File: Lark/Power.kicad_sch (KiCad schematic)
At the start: 0 parts

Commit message: added power section to schematic
It needs revised, due to thermal issue. Specifically in regards to my soft start circuit, the mosfet wont be able to handle the power dissipated during a slow turn on.
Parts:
- added C20, C23, C29: 0.1µF, Murata Electronics:C_0603, symbol Murata Electronics:Capacitor
- added C21: 4.7µF, Murata Electronics:C_0603, symbol Murata Electronics:Capacitor
- added C22: 22µF, Murata Electronics:C_0603, symbol Murata Electronics:Capacitor
- added C24: 6800pF, Murata Electronics:C_0603, symbol Murata Electronics:Capacitor
- added C25: 18pF, Murata Electronics:C_0603, symbol Murata Electronics:Capacitor
- added C26, C27, C28, C32: 22µF, TDK Corporation:C2012X5R1V226M125AC, symbol TDK Corporation:C2012X5R1V226M125AC
- added C30, C31: 10µF, Murata Electronics:C_0603, symbol Murata Electronics:Capacitor
- added D17: SS26FL, onsemi:SS26FL, symbol onsemi:SS26FL
- added D18: LTST-C171GKT, Lite-On Inc:LED_0805, symbol Lite-On Inc:LTST-C171GKT
- added F1: 7A Slow Blow, SCHURTER Inc:3413.0326.22, symbol SCHURTER Inc:3413.0326.22
- added J8: 54-00128, Tensility International Corp:54-00128, symbol Tensility International Corp:54-00128
- added L1: 15µH, TDK Corporation:CLF5030NIT-150M-D, symbol TDK Corporation:CLF5030NIT-150M-D
- added L2: 4.7µH, TDK Corporation:CLF7045NIT-4R7N-D, symbol TDK Corporation:CLF7045NIT-4R7N-D
- added Q1: SISS65DN-T1-GE3, Vishay Siliconix:SISS65DN-T1-GE3, symbol Vishay Siliconix:SISS65DN-T1-GE3
- added Q2: MMBT2222A-7-F, Diodes Incorporated:MMBT2222A-7-F, symbol Diodes Incorporated:MMBT2222A-7-F
- added R43, R45: 15kΩ, Stackpole:R_0603, symbol Stackpole:Resistor
- added R44: 51kΩ, Stackpole:R_0603, symbol Stackpole:Resistor
- added R46: 100kΩ, Stackpole:R_0603, symbol Stackpole:Resistor
- added R47: 402kΩ, Stackpole:R_0603, symbol Stackpole:Resistor
- added R48, R53: 10KΩ, Stackpole:R_0603, symbol Stackpole:Resistor
- added R49: 20KΩ, Stackpole:R_0603, symbol Stackpole:Resistor
- added R50: 100KΩ, Stackpole:R_0603, symbol Stackpole:Resistor
- added R51: 1KΩ, Stackpole:R_0603, symbol Stackpole:Resistor
- added R52: 220Ω, Stackpole:R_2512, symbol Stackpole:Resistor
- added TP10, TP11, TP12, TP8, TP9: TestPoint, TestPoint:TestPoint_Pad_D1.0mm, symbol Connector:TestPoint
- added U11: BD9G102G-LBTR, ROHM:BD9G102G-LBTR, symbol ROHM:BD9G102G-LBTR
- added U12: BD9E302EFJ-E2, ROHM:BD9E302EFJ-E2, symbol ROHM:BD9E302EFJ-E2
- added U13: LD39200PU33R, STMicroelectronics:LD39200PU33R, symbol STMicroelectronics:LD39200PU33R
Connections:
- new net: F1.1, J8.1
- new net: C32.2, Q1.4 (G), R48.2, R49.1
- new net: Q2.3 (C), R49.2
- new net: C24.1, R45.1
- new net: C20.2, D17.1 (K), L1.1, U11.6 (LX)
- new net: Q2.1 (B), R51.2
- new net: C20.1, U11.1 (BST)
- new net: D18.1 (K), R53.1
- new net +24V: C28.1, C29.2, D18.2 (A), Q1.5 (D1), Q1.6 (D2), Q1.7 (D3), Q1.8 (D4), R52.1, TP11.1, U12.2 (VIN), U12.3 (EN)
- new net +24VBC: C21.1, C32.1, F1.2, Q1.1 (S1), Q1.2 (S2), Q1.3 (S3), R48.1, TP10.1, U11.4 (EN), U11.5 (VCC)
- new net +3.3V: C31.1, TP8.1, U13.1 (OUT), U13.2 (SENSE)
- new net +3.3VBC: C22.1, L1.2, R44.1, TP12.1
- new net +4V: C25.2, C26.1, C27.1, C30.1, L2.1, R47.1, TP9.1, U13.5 (EN), U13.6 (IN)
- new net BOOT: C23.1, U12.1 (BOOT)
- new net COMP: C24.2, U12.6 (COMP)
- new net Drain: J8.3, R52.2
- new net FB_1: R43.1, R44.2, U11.3 (FB)
- new net FB_2: C25.1, R46.1, R47.2, U12.5 (FB)
- new net GND: C21.2, C22.2, C26.2, C27.2, C28.2, C29.1, C30.2, C31.2, D17.2 (A), J8.2, Q2.2 (E), R43.2, R45.2, R46.2, R50.2, R53.2, U11.2 (GND), U12.4 (AGND), U12.7 (PGND), U12.9 (EP), U13.3 (GND), U13.7 (EP)
- new net PWR_EN: R50.1, R51.1
- new net SW: C23.2, L2.2, U12.8 (SW)
- no-connect marks 0 -> 1
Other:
- note added: "6800µF Bulk Cap Drain Time 5 Sec @ 100mA"
- note added: "ATTiny Boot Controller Supply"
- note added: "Main Buck Regulator"
- note added: "Main Linear Voltage Regulator"
- note added: "Power Entry"
- note added: "Power Test Points"

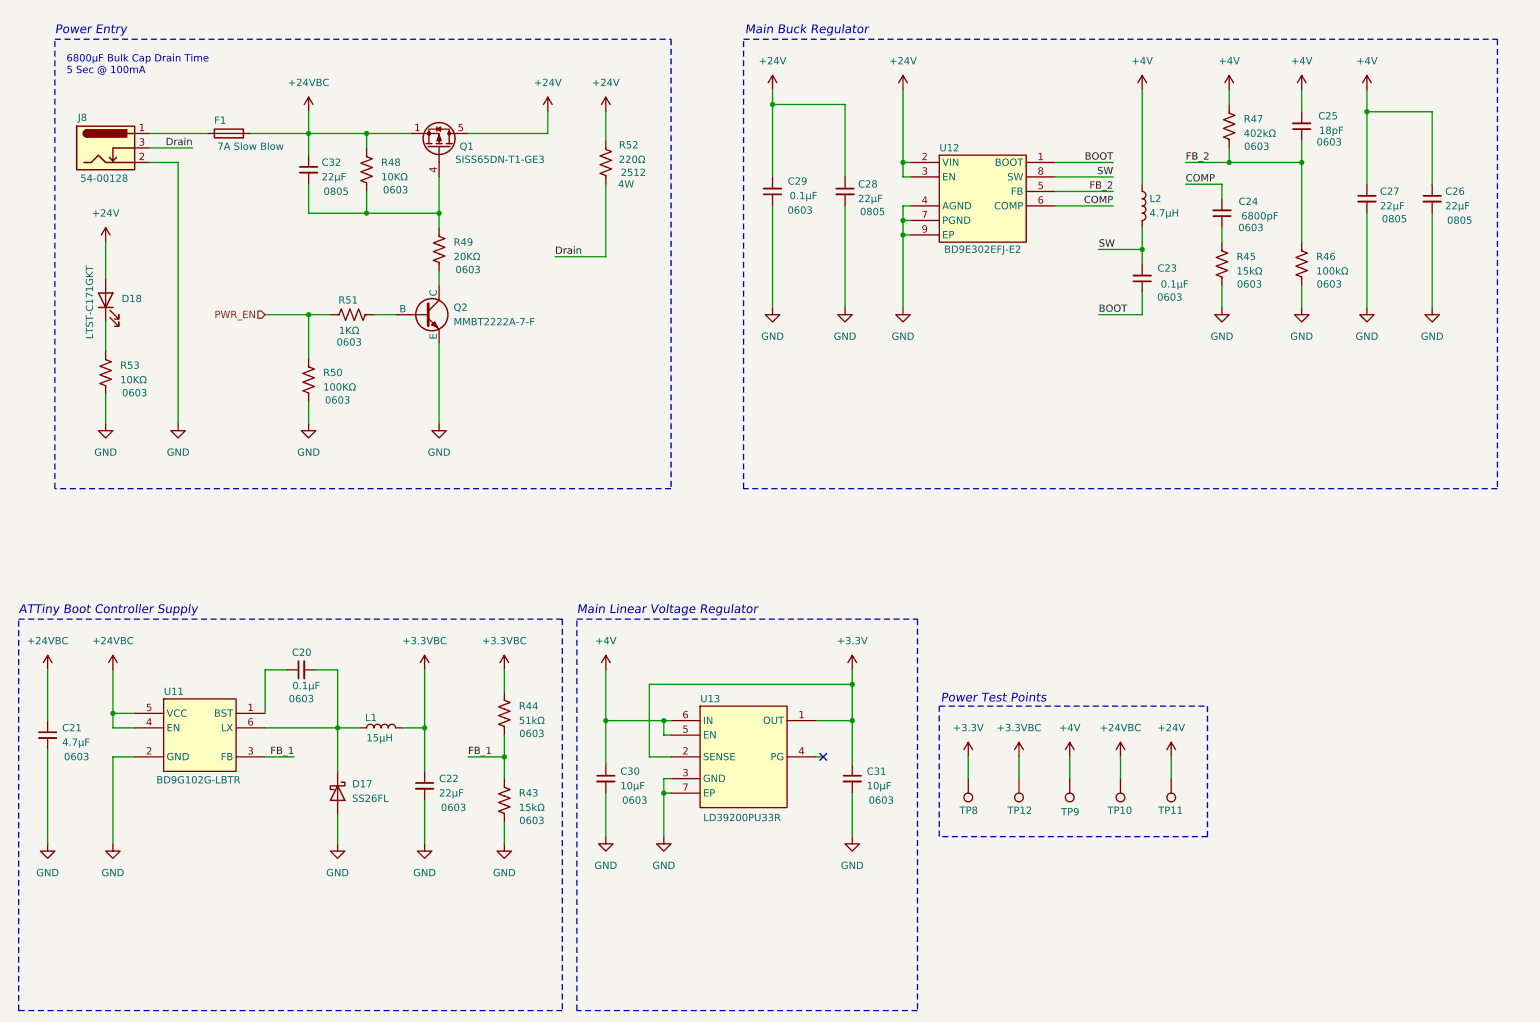
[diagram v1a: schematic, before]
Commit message: update, WIP
- Reannotated schematic.
- Added STM32 device.
- Fixed High-side switch (removed soft-start cap for device safety).
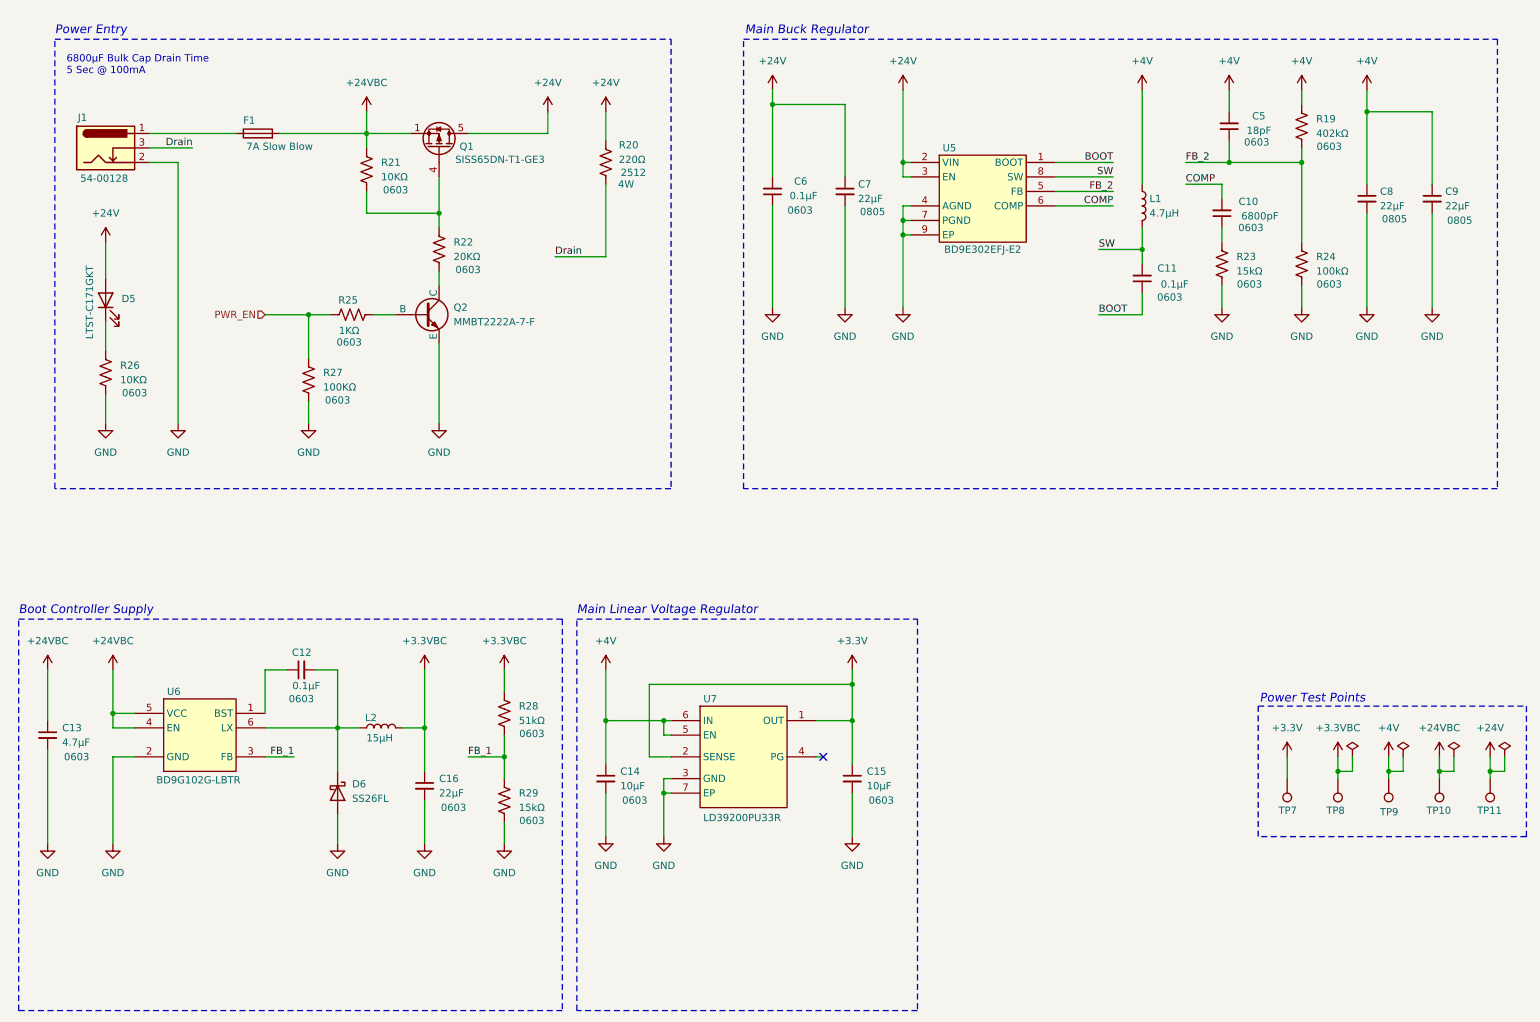
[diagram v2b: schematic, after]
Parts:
- removed C32: 22µF, TDK Corporation:C2012X5R1V226M125AC, symbol TDK Corporation:C2012X5R1V226M125AC
- renumbered C24 to C10, C23 to C11, C20 to C12, C21 to C13, C30 to C14, C31 to C15, C22 to C16, C25 to C5, C29 to C6, C28 to C7, C27 to C8, C26 to C9, D18 to D5, D17 to D6, J8 to J1, L2 to L1, L1 to L2, R47 to R19, R52 to R20, R48 to R21, R49 to R22, R45 to R23, R46 to R24, R51 to R25, R53 to R26, R50 to R27, R44 to R28, R43 to R29, TP8 to TP7, TP12 to TP8, U12 to U5, U11 to U6, U13 to U7
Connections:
- net GND: now also J1.SH1, J1.SH2
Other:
- note added: "Boot Controller Supply"
- note removed: "ATTiny Boot Controller Supply"
- moved on the sheet: C5, F1, R19, TP10, TP11, TP7, TP8, TP9

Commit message: Updated schematic, WIP
- Added NOR flash part.
- Added new CubeMX config file.
- Reannotated the schematic.
- Made some more connections to the MCU.
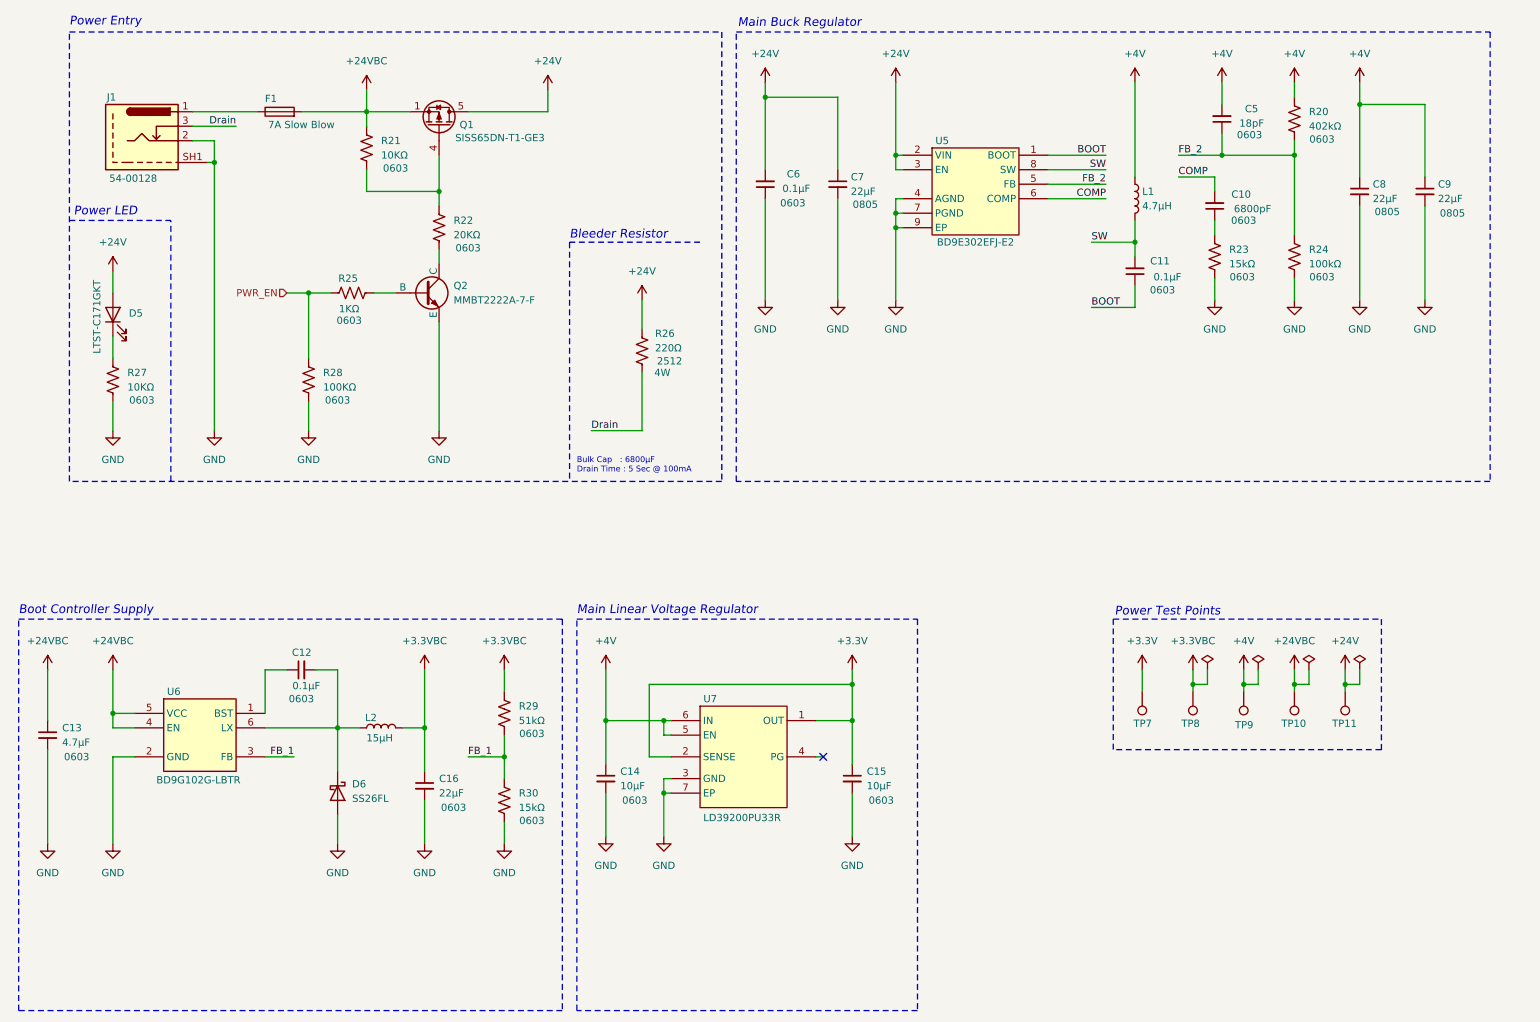
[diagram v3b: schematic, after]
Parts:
- renumbered R19 to R20, R20 to R26, R26 to R27, R27 to R28, R28 to R29, R29 to R30
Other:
- note added: "Bleeder Resistor"
- note added: "Bulk Cap : 6800µF Drain Time : 5 Sec @ 100mA"
- note added: "Power LED"
- note removed: "6800µF Bulk Cap Drain Time 5 Sec @ 100mA"
- moved on the sheet: C10, C11, C5, C6, C7, C8, C9, D5, F1, L1, Q1, Q2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

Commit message: Update, WIP
- Added TVS diode to 24v Supply.
- Fixed bleeder circuit at some point (I think it was this commit)
- Added Jumper to connect NTC to ADC. (again I think it was this commit)
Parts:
- added D20: SZSMF6L28AT3G, Littelfuse Inc:SZSMF6L28AT3G, symbol Littelfuse Inc:SZSMF6L28AT3G
- added D6: BZT52C10T-7, Diodes Incorporated:BZT52C10T-7, symbol Diodes Incorporated:BZT52C10T-7
- added Q3: MMBF170, onsemi:MMBF170, symbol onsemi:MMBF170
- added Q4: MMBT2222A-7-F, Diodes Incorporated:MMBT2222A-7-F, symbol Diodes Incorporated:MMBT2222A-7-F
- added R28: 10KΩ, Stackpole:R_0603, symbol Stackpole:Resistor
- added R30: 100Ω, Stackpole:R_0603, symbol Stackpole:Resistor
- added R32: 1KΩ, Stackpole:R_0603, symbol Stackpole:Resistor
- renumbered D6 to D7, R27 to R26, R28 to R27, R26 to R29, R29 to R31, R30 to R33
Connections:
- net +24VBC: now also D20.1 (Cathode), R28.1
- net GND: now also D20.2 (Anode), D6.2 (A), Q3.2 (S), Q4.2 (E)
- net PWR_EN: now also R32.1
- net Drain: no longer names the net of R29.2
- net Drain: now also Q3.3 (D); no longer J1.3
- new net: D6.1 (K), Q4.3 (C), R28.2, R30.1
- new net: Q4.1 (B), R32.2
- new net: Q3.1 (G), R30.2
- no-connect marks 1 -> 2
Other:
- note added: "Bleeder Circuit"
- note added: "Circuit Protection"
- note added: "Test Points"
- note added: "When Power En = High - The 24V Rail is Active When Power En = Low - The 24V Rail is Inactive"
- note added: "When Power En = High - The Bleed Resistor is Floating When Power En = Low - The Bleed Resistor is Connected to GND."
- note removed: "Bleeder Resistor"
- note removed: "Power Test Points"
- moved on the sheet: C10, C11, C12, C13, C16, C5, C6, C7, C8, C9, D5, D7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

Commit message: updated WIP
- fixed high-side switch (swapped out pfets)
- swapped out bleeder fet.
- changed a few footprints.
- changed zeners to 15v ones
- added soft-start cap back in to the high-side switch.

(today ive mainly been struggling with the inrush current, but I think its solved now)
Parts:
- removed Q1: SISS65DN-T1-GE3, Vishay Siliconix:SISS65DN-T1-GE3, symbol Vishay Siliconix:SISS65DN-T1-GE3
- removed Q3: MMBF170, onsemi:MMBF170, symbol onsemi:MMBF170
- added C6: 22µF, TDK Corporation:C2012X5R1V226M125AC, symbol TDK Corporation:C2012X5R1V226M125AC
- added D6: BZT52C15T-7, Diodes Incorporated:BZT52C10T-7, symbol Diodes Incorporated:BZT52C10T-7
- added U5: SQM120P06-07L_GE3, Vishay Siliconix:SQM120P06-07L_GE3, symbol Vishay Siliconix:SQM120P06-07L_GE3
- added U7: SI3474DV-T1-BE3, Vishay Siliconix:SI3474DV-T1-BE3, symbol Vishay Siliconix:SI3474DV-T1-BE3
- D8: renamed from D6; value BZT52C10T-7 -> BZT52C15T-7
- F1: value 7A Slow Blow -> 8A Slow Blow
- renumbered C9 to C10, C10 to C11, C11 to C12, C12 to C13, C13 to C14, C14 to C15, C15 to C16, C16 to C17, C6 to C7, C7 to C8, C8 to C9, D20 to D5, D5 to D7, D7 to D9, Q2 to Q1, Q4 to Q2, U5 to U6, U6 to U8, U7 to U9
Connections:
- net +24V: now also U5.2 (D)
- net +24VBC: now also C6.1, D6.1 (K), U5.3 (S)
- net GND: now also U7.4 (S)
- net at R21.2, R22.1: now also C6.2, D6.2 (A), U5.1 (G)
- net at R30.2: now also U7.3 (G)
- net at R29.2: now also U7.1 (D1), U7.2 (D2), U7.5 (D3), U7.6 (D4)
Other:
- note added: "100ms Start-Up Delay"
- note removed: "Circuit Protection"
- moved on the sheet: D5, D8, F1, Q2, R28, R29, R30, R32, TP10, TP11, TP7, TP8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
